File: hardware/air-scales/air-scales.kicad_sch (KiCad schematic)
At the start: 73 parts, among them J1 Connector, USB-TYPE-C-16P, J3 Conn_02x02_Odd_Even, J4 Conn_02x02_Odd_Even, J6 Conn_02x01, Q1 C458246, SW1 B3FS-1000, SW2 B3FS-1000, U1 BME280, U2 TPS62162DSG, U3 SMA6T28AY, U4 SMA6T15AY, U5 LM74610QDGKTQ1, U6 LM63625DQPWPRQ1, U7 TPS2553DRVR, U8 TPS2121RUXR, U9 ESP32-S3-WROOM-1U-N16R8

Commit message: pcb placement is done round 1
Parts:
- added D3: ESD441DPLR, PCM_JLCPCB:D_SOD-123FL, symbol PCM_JLCPCB-Diodes:TVS-Uni,SMF20A
- renumbered D3 to D10
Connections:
- net -12V BATT is gone; now on net GND: C1.2, C10.2, C11.2, C12.2, C13.2, C14.2, C15.2, C16.2, C17.2, C18.2, C19.2, C2.2, C20.2, C21.2, C22.2, C23.2, C24.2, C25.2, C26.2, C3.2, C5.2, C6.2, C7.2, C8.2, D1.1, D10.1, D2.1, D4.1 (K), D5.1, D6.1, D7.1, D8.1, D9.3 (GND), J1.A12B1 (GND), J1.B12A1 (GND), J1.S1 (SHIELD), J3.1 (Pin_1), J4.2 (Pin_2), J6.2 (Pin_2), R1.2, R15.2, R2.2, R4.2, R8.2, R9.2, SW1.3, SW1.4, SW2.3, SW2.4, U1.1 (GND), U1.5 (SDO), U1.7 (GND), U2.1 (PGND), U2.4 (AGND), U2.5 (FB), U3.2 (A), U4.1 (K), U6.10 (AGND), U6.15 (PGND), U6.16 (PGND), U6.17 (PAD), U6.5 (RT), U6.7 (SYNC_MODE), U7.5 (GND), U8.12 (GND), U8.4 (OV2), U8.5 (OV1), U9.1 (GND), U9.40 (GND__1), U9.41_1 (GND__2), U9.41_2 (GND__3), U9.41_3 (GND__4), U9.41_4 (GND__5), U9.41_5 (GND__6), U9.41_6 (GND__7), U9.41_7 (GND__8), U9.41_8 (GND__9), U9.41_9 (GND__10)
- net PRESSURE_IN: now also U9.25 (IO48); no longer U9.4 (IO4)
- net SCL: now also U9.17 (IO9); no longer U9.12 (IO8)
- net SDA: now also U9.16 (IO46); no longer U9.17 (IO9)
- net U0RXD: now also U9.22 (IO14); no longer U9.36 (RXD0)
- net U0TXD: now also U9.21 (IO13); no longer U9.37 (TXD0)
- net at C12.1, J1.A9B4 (VBUS), J1.B9A4 (VBUS)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: now also D3.2
- net GND: now reaches U2.9 (PAD)
- net GND: now also D3.1
- net CC1: no longer names the net of J1.A5 (CC1), R2.1
- net CC2: no longer names the net of J1.B5 (CC2), R1.1
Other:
- moved on the sheet: D1, D10, D2, R1, R2

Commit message: added pwr_flag to the power lines???
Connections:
- net GND: no longer C2.2, D5.1, U3.2 (A), U4.1 (K)
- new net: C2.2, D5.1, U3.2 (A), U4.1 (K)
- no-connect marks 0 -> 9

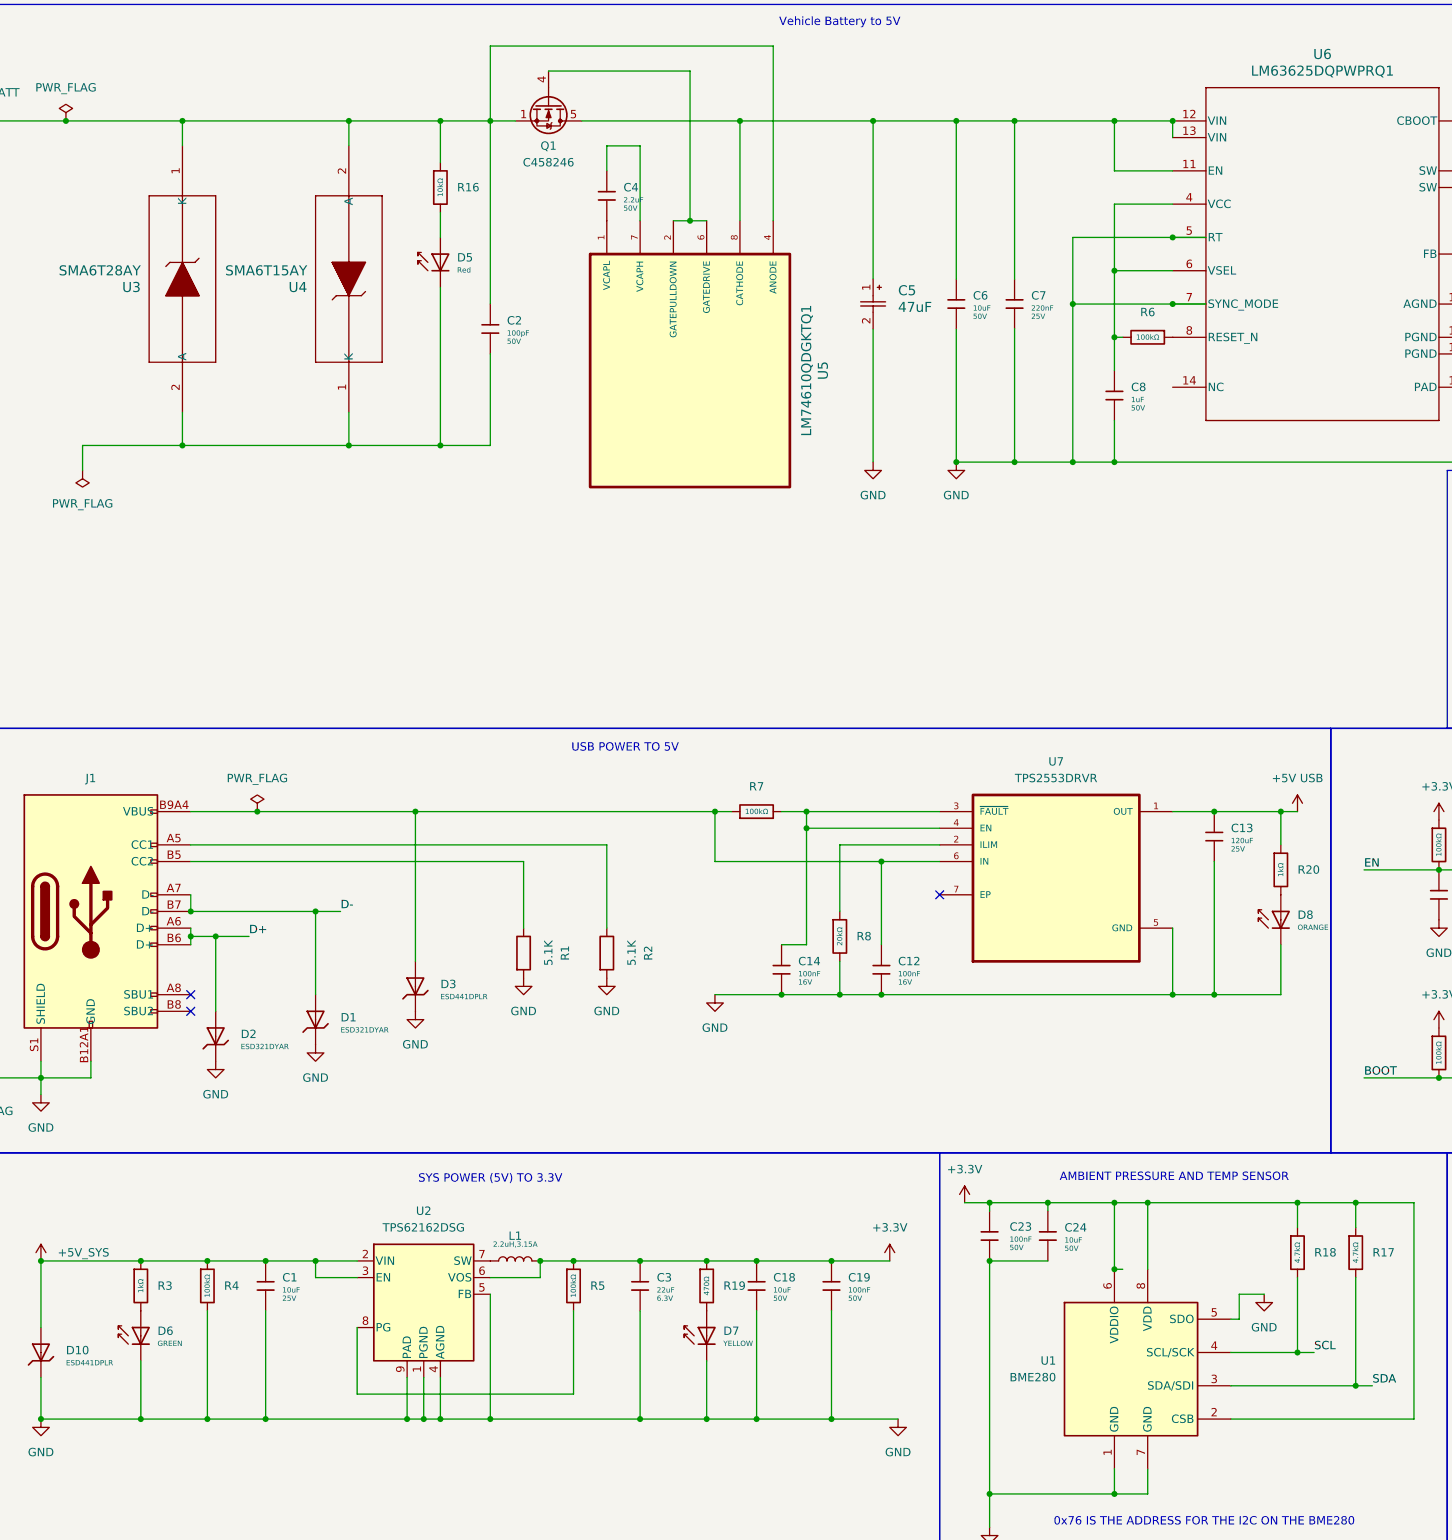
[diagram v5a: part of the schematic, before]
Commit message: added pwr_flag to the power lines???
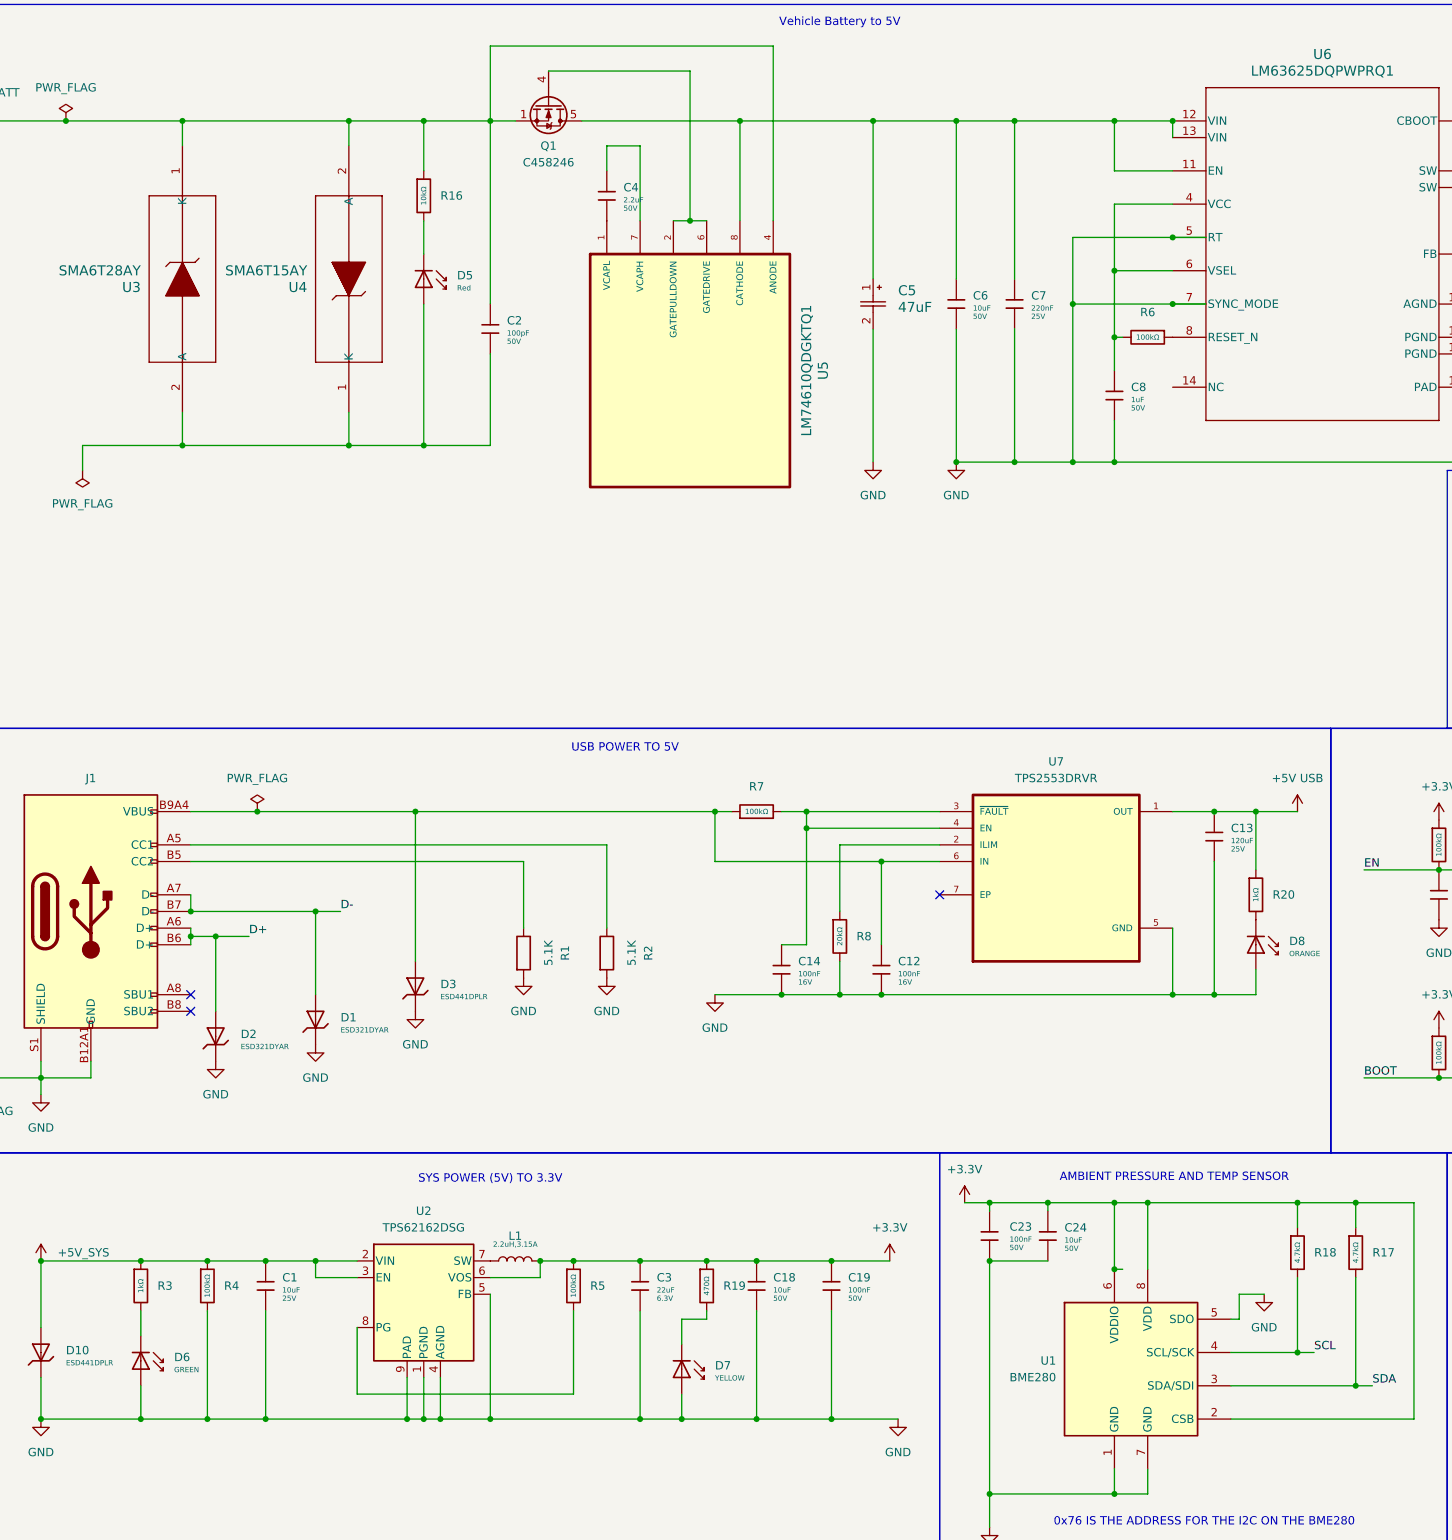
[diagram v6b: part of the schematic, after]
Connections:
- net GND: now also D6.2, D7.2, D8.2; no longer D6.1, D7.1, D8.1
- net at R3.2: now also D6.1; no longer D6.2
- net at C2.2, U3.2 (A), U4.1 (K): now also D5.2; no longer D5.1
- net at R19.2: now also D7.1; no longer D7.2
- net at R16.2: now also D5.1; no longer D5.2
- net at R20.2: now also D8.1; no longer D8.2
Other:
- moved on the sheet: D5, D6, D7, D8, R16, R20

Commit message: need to redo a bunch of shit - lots of errors, totally fucked this all up
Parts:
- removed C15: 100nF, PCM_JLCPCB:C_0402, symbol PCM_JLCPCB-Capacitors:0402,100nF
- removed D6: GREEN, PCM_JLCPCB:D_0603, symbol PCM_JLCPCB-Diodes:LED,0603,Red
- removed R3: 1kΩ, PCM_JLCPCB:R_0603, symbol PCM_JLCPCB-Resistors:0603,3.3kΩ
- removed R4: 100kΩ, PCM_JLCPCB:R_0603, symbol PCM_JLCPCB-Resistors:0603,100kΩ
- added C27, C28, C29: 100nF, PCM_JLCPCB:C_0603, symbol PCM_JLCPCB-Capacitors:0603,100nF
- added C30: 22uF, PCM_JLCPCB:C_1206, symbol PCM_JLCPCB-Capacitors:1206,22uF,(2)
- added D11: BLUE, PCM_JLCPCB:D_0603, symbol PCM_JLCPCB-Diodes:LED,0603,Red
- added D12: ORANGE, PCM_JLCPCB:D_0603, symbol PCM_JLCPCB-Diodes:LED,0603,Red
- added R21, R22: 1.5kΩ, PCM_JLCPCB:R_0603, symbol PCM_JLCPCB-Resistors:0603,3.3kΩ
- added R3: 10kΩ, PCM_JLCPCB:R_0603, symbol PCM_JLCPCB-Resistors:0603,10kΩ
- D5: value Red -> RED
- D7: value YELLOW -> GREEN
- R16: value 10kΩ -> 5kΩ; LCSC C25804 -> (none); Price 0.004USD -> (none); Resistance 10kΩ -> 5kΩ; Stock 51181774 -> (none)
- R19: value 470Ω -> 650Ω
- R20: value 1kΩ -> 1.5kΩ
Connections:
- net +12V BATT: no longer R16.1
- net +5V VEHICLE: now also R20.1, U8.7_1 (IN1__1), C27.1; no longer U8.6 (PR1)
- net +5V_SYS: now also C13.1, U7.1 (OUT), R21.1; no longer C17.1, U8.1 (OUT), U8.1_1 (OUT__1), U8.8 (OUT__2), U8.8_1 (OUT__3)
- net GND: now also C2.2, D5.2, U3.2 (A), U4.1 (K), U8.3 (CP2), U8.6 (PR1), U8.9 (ST), C27.2, C28.2, C29.2, C30.2, D11.2, D12.2
- net LED: now also U9.21 (IO13); no longer U9.5 (IO5)
- net PRESSURE_IN: now also U9.29 (IO36); no longer U9.25 (IO48)
- net SCL: now also U9.33 (IO40); no longer U9.17 (IO9)
- net SDA: now also U9.32 (IO39); no longer U9.16 (IO46)
- net U0RXD: now also J3.2 (Pin_2), U9.36 (RXD0); no longer J3.3 (Pin_3), U9.22 (IO14)
- net U0TXD: now also J3.3 (Pin_3), U9.37 (TXD0); no longer J3.2 (Pin_2), U9.21 (IO13)
- net +12VA: now reaches C5.1, C6.1, C7.1, Q1.5 (D), U5.8 (CATHODE), U6.11 (EN), U6.12 (VIN), U6.13 (VIN)
- net +12VA: now also R16.1
- net at U5.1 (VCAPL): now also C4.1; no longer C4.2
- net at U5.7 (VCAPH): now also C4.2; no longer C4.1
- net +5V ARB: now reaches C12.1, R7.1, U7.6 (IN)
- net +5V ARB: now also C14.1, C17.1, U8.1 (OUT), U8.1_1 (OUT__1), U8.8 (OUT__2), U8.8_1 (OUT__3), C29.1, C30.1, R22.1, R3.1; no longer D3.2, J1.A9B4 (VBUS), J1.B9A4 (VBUS)
- net at R7.2, U7.3 (~{FAULT}): no longer C14.1, U7.4 (EN)
- net VBUS: now reaches U8.2_1 (IN2__1)
- net VBUS: now also C26.1, D3.2, J1.A9B4 (VBUS), J1.B9A4 (VBUS), U8.2 (IN2), C28.1
- removed net +5V USB: C13.1, C26.1, R20.1, U7.1 (OUT), U8.2 (IN2)
- new net: D12.1, R22.2
- new net: R3.2, U7.4 (EN)
- new net: D11.1, R21.2
- no-connect marks 9 -> 7
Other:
- note added: "0x76 ADDRESS SET BY SDO TO GND"
- note added: "LED"
- note added: "LM74610-Q1 Zero IQ Reverse Polarity Protection Smart Diode Controller"
- note added: "Precision Adjustable Current-Limited Power-Distribution Switches SET TO 1.1AMP AT 5V BY R8"
- note added: "STEP DOWN VOLTAGE CONVERTER WITH SPREAD SPECTRUM"
- note added: "USB C"
- note removed: "0x76 IS THE ADDRESS FOR THE I2C ON THE BME280"
- note removed: "USB POWER TO 5V"
- note removed: "Vehicle Battery to 5V"
- moved on the sheet: C1, C10, C11, C12, C13, C14, C16, C17, C18, C19, C2, C20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

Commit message: PCB done????
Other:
- note added: "X"
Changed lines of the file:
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@@
 		)
 	)
+	(text "X"
+		(exclude_from_sim no)
+		(at 177.038 132.842 0)
+		(effects
+			(font
+				(size 12.7 12.7)
+			)
+		)
+	)
 	(text "STEP DOWN VOLTAGE CONVERTER WITH SPREAD SPECTRUM"
 		(exclude_from_sim no)
@@
 		)
 	)
+	(text "X"
+		(exclude_from_sim no)
+		(at 80.01 135.89 0)
+		(effects
+			(font
+				(size 12.7 12.7)
+			)
+		)
+	)
 	(text "LM74610-Q1 Zero IQ Reverse Polarity Protection Smart Diode Controller\n"
 		(exclude_from_sim no)
@@
 			(at 69.85 30.48 0)
 			(effects
+				(font
+					(size 1.27 1.27)
+				)
+				(hide yes)
+			)
+		)
+		(property "Manufacturer" ""
+			(at 69.85 30.48 0)
+			(effects
+				(font
+					(size 1.27 1.27)
+				)
+				(hide yes)
+			)
+		)
+		(property "Mfr. Part #" ""
+			(at 69.85 30.48 0)
+			(effects
+				(font
+					(size 1.27 1.27)
+				)
+				(hide yes)
+			)
+		)
+		(property "LCSC" ""
+			(at 69.85 30.48 0)
+			(effects
